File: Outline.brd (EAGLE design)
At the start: 53.8 x 53.8 mm, 51 parts, among them CN1 0675031020, IC1 ATXMEGA32A4U-AU, IC2 ST1480ACDR, J1 RJHSE5080, J2 J2, U1 NCP1117DTAG @ 3.3v, U2 NCP1117DTAG @ 12v

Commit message: 4.1d
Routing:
- net RS485_P: track 68.4 -> 70.6 mm
- net GND: track 16.3 -> 17.0 mm
- net TX: track 10.5 -> 9.92 mm

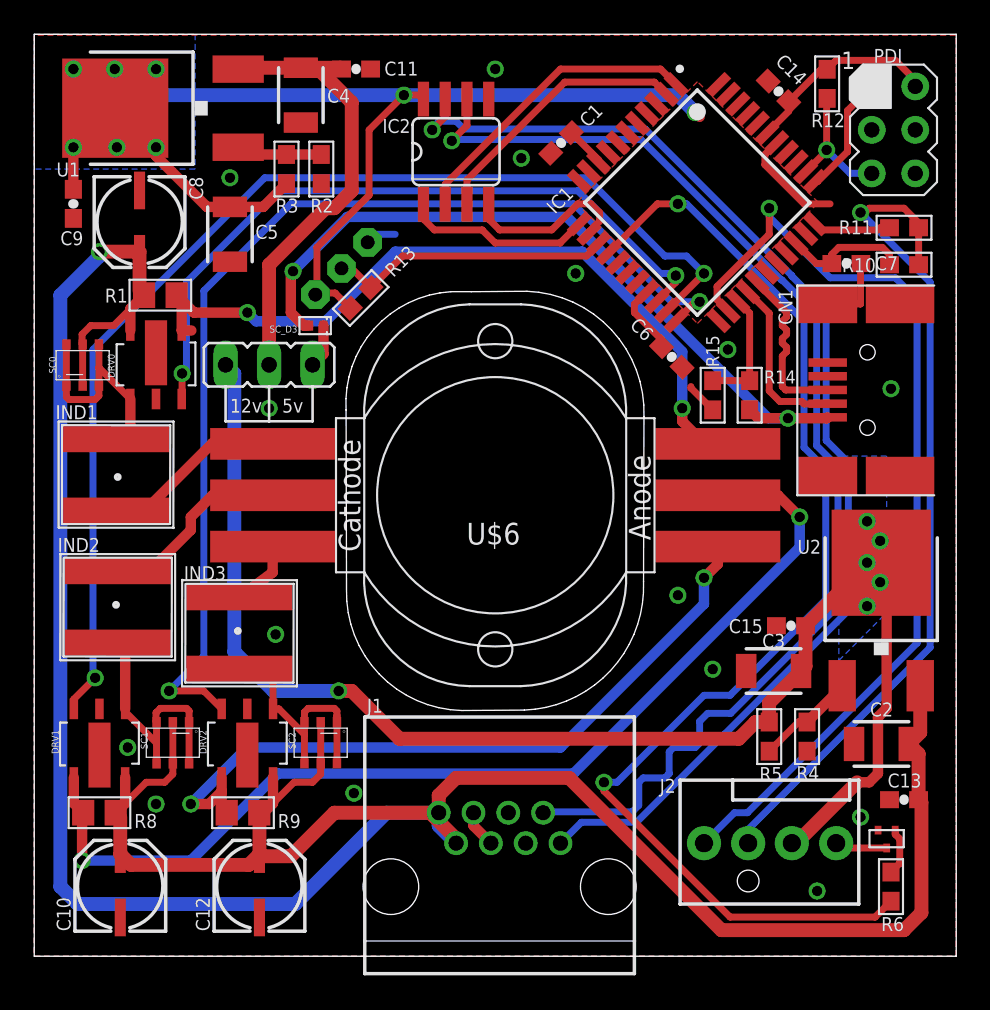
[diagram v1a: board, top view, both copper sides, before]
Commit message: 4.2
Rounded Corners with some final touch up.
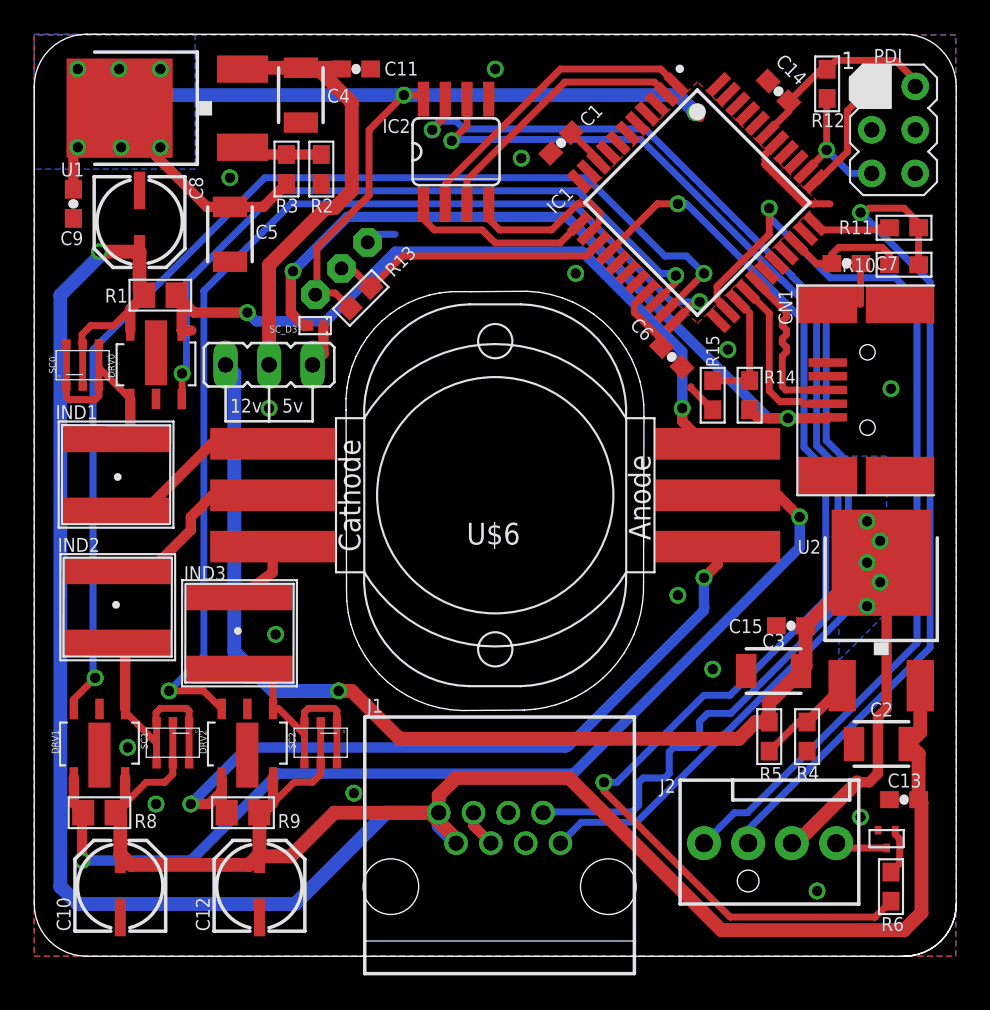
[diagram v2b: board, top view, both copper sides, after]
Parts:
- moved U1 0.25 mm to (7.37, 49.5)
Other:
- outline, holes or cut-outs redrawn
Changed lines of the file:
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@@
 <board>
 <plain>
-<wire x1="0" y1="0" x2="53.848" y2="0" width="0" layer="20"/>
-<wire x1="53.848" y1="0" x2="53.848" y2="53.848" width="0" layer="20"/>
-<wire x1="53.848" y1="53.848" x2="0" y2="53.848" width="0" layer="20"/>
-<wire x1="0" y1="53.848" x2="0" y2="0" width="0" layer="20"/>
+<wire x1="3.048" y1="0" x2="50.8" y2="0" width="0" layer="20"/>
+<wire x1="53.848" y1="3.048" x2="53.848" y2="50.8" width="0" layer="20"/>
+<wire x1="50.8" y1="53.848" x2="3.048" y2="53.848" width="0" layer="20"/>
 <polygon width="0.0508" layer="20" spacing="48.26" pour="hatch">
 <vertex x="25.527" y="38.8112"/>
@@
 <vertex x="50.038" y="49.53"/>
 </polygon>
+<wire x1="0" y1="50.8" x2="0" y2="3.048" width="0" layer="20"/>
 <wire x1="11.176" y1="33.274" x2="11.176" y2="31.242" width="0.1524" layer="25"/>
 <wire x1="13.716" y1="33.274" x2="13.716" y2="31.242" width="0.1524" layer="25"/>
@@
 <text x="11.43" y="31.75" size="0.8128" layer="25">12v</text>
 <text x="14.478" y="31.75" size="0.8128" layer="25">5v</text>
-<text x="3.302" y="46.736" size="1.27" layer="26" font="vector" rot="MR270">http://TechIsCool.com</text>
-<text x="5.334" y="52.832" size="1.27" layer="26" font="vector" rot="MR270">High Brightness RGB LED Driver</text>
-<text x="7.366" y="52.832" size="1.27" layer="26" font="vector" rot="MR270">Copyright 2012 TechIsCool v1.0</text>
+<text x="4.064" y="39.624" size="1.27" layer="26" font="vector" rot="MR270">http://TechIsCool.com</text>
+<text x="5.842" y="46.482" size="1.27" layer="26" font="vector" rot="MR270">High Brightness RGB LED Driver</text>
+<text x="7.62" y="49.022" size="1.27" layer="26" font="vector" rot="MR270">Copyright 2012 TechIsCool v1.0</text>
+<wire x1="0" y1="50.8" x2="3.048" y2="53.848" width="0" layer="20" curve="-90"/>
+<wire x1="53.848" y1="50.8" x2="50.8" y2="53.848" width="0" layer="20" curve="90"/>
+<wire x1="50.8" y1="0" x2="53.848" y2="3.048" width="0" layer="20" curve="90"/>
+<wire x1="50.8" y1="0" x2="53.848" y2="3.048" width="0" layer="20" curve="90"/>
+<wire x1="0" y1="3.048" x2="3.048" y2="0" width="0" layer="20" curve="90"/>
 </plain>
 <attributes>
@@
 <attribute name="NAME" x="12.916" y="41.902" size="0.8128" layer="25"/>
 </element>
-<element name="U1" library="SparkFun" package="V-REG_DPACK" value="NCP1117DTAG @ 3.3v" x="7.112" y="49.53" smashed="yes" rot="R90">
-<attribute name="NAME" x="2.667" y="46.355" size="0.8128" layer="25" rot="R180"/>
+<element name="U1" library="SparkFun" package="V-REG_DPACK" value="NCP1117DTAG @ 3.3v" x="7.366" y="49.53" smashed="yes" rot="R90">
+<attribute name="NAME" x="2.921" y="46.355" size="0.8128" layer="25" rot="R180"/>
 </element>
 <element name="U2" library="SparkFun" package="V-REG_DPACK" value="NCP1117DTAG @ 12v" x="49.4664" y="20.6" smashed="yes">
@@
 <via x="21.59" y="50.292" extent="1-16" drill="0.6"/>
 <wire x1="2.286" y1="44.792" x2="2.286" y2="47.084" width="0.6096" layer="1"/>
-<wire x1="4.732" y1="49.53" x2="4.732" y2="49.116" width="0.6096" layer="1"/>
-<via x="2.286" y="47.244" extent="1-16" drill="0.6"/>
-<via x="4.826" y="47.244" extent="1-16" drill="0.6"/>
-<via x="7.112" y="47.244" extent="1-16" drill="0.6"/>
-<via x="7.112" y="51.816" extent="1-16" drill="0.6"/>
-<via x="4.699" y="51.816" extent="1-16" drill="0.6"/>
-<via x="2.286" y="51.816" extent="1-16" drill="0.6"/>
-<wire x1="2.286" y1="47.084" x2="2.286" y2="47.244" width="0.8128" layer="1"/>
+<wire x1="4.986" y1="49.53" x2="4.732" y2="49.116" width="0.6096" layer="1"/>
+<via x="2.54" y="47.244" extent="1-16" drill="0.6"/>
+<via x="5.08" y="47.244" extent="1-16" drill="0.6"/>
+<via x="7.366" y="47.244" extent="1-16" drill="0.6"/>
+<via x="7.366" y="51.816" extent="1-16" drill="0.6"/>
+<via x="4.953" y="51.816" extent="1-16" drill="0.6"/>
+<via x="2.54" y="51.816" extent="1-16" drill="0.6"/>
+<wire x1="2.286" y1="47.084" x2="2.54" y2="47.244" width="0.8128" layer="1"/>
 <wire x1="46.5821" y1="40.4558125" x2="46.5821" y2="40.9941" width="0.4064" layer="1"/>
 <wire x1="46.5821" y1="40.9941" x2="46.99" y2="41.402" width="0.4064" layer="1"/>
@@
 <wire x1="22.5044" y1="50.292" x2="22.733" y2="50.0634" width="0.4064" layer="1"/>
 <wire x1="10.084" y1="43.764" x2="7.112" y2="46.736" width="0.6096" layer="1"/>
-<wire x1="7.112" y1="46.736" x2="7.112" y2="47.244" width="0.6096" layer="1"/>
+<wire x1="7.112" y1="46.736" x2="7.366" y2="47.244" width="0.6096" layer="1"/>
 <wire x1="16.51" y1="38.734996875" x2="17.572121875" y2="38.734996875" width="0.4064" layer="1"/>
 <wire x1="17.572121875" y1="38.734996875" x2="18.4643625" y2="37.84275625" width="0.4064" layer="1"/>
@@
 <wire x1="19.558" y1="44.45" x2="19.558" y2="48.26" width="0.4064" layer="1"/>
 <wire x1="19.558" y1="48.26" x2="21.59" y2="50.292" width="0.4064" layer="1"/>
-<wire x1="4.826" y1="47.244" x2="4.826" y2="49.436" width="0.4064" layer="1"/>
-<wire x1="4.826" y1="49.436" x2="4.732" y2="49.53" width="0.4064" layer="1"/>
+<wire x1="5.08" y1="47.244" x2="4.826" y2="49.436" width="0.4064" layer="1"/>
+<wire x1="4.826" y1="49.436" x2="4.986" y2="49.53" width="0.4064" layer="1"/>
 <wire x1="37.592" y1="50.292" x2="21.59" y2="50.292" width="0.8128" layer="16"/>
 <wire x1="21.59" y1="50.292" x2="7.112" y2="50.292" width="0.8128" layer="16"/>
-<wire x1="7.112" y1="50.292" x2="7.112" y2="51.816" width="0.8128" layer="16"/>
+<wire x1="7.112" y1="50.292" x2="7.366" y2="51.816" width="0.8128" layer="16"/>
 </signal>
 <signal name="N$1">
@@
 <wire x1="16.764" y1="46.824" x2="14.732" y2="46.824" width="0.6096" layer="1"/>
 <wire x1="14.732" y1="46.824" x2="12.338" y2="46.824" width="0.6096" layer="1"/>
-<wire x1="12.338" y1="46.824" x2="11.912" y2="47.25" width="0.6096" layer="1"/>
+<wire x1="12.338" y1="46.824" x2="12.166" y2="47.25" width="0.6096" layer="1"/>
 </signal>
 <signal name="GND">
@@
 <contactref element="C4" pad="1"/>
 <contactref element="JP1" pad="2"/>
-<wire x1="11.912" y1="51.81" x2="11.9568" y2="51.5112" width="0.6096" layer="1"/>
+<wire x1="12.166" y1="51.81" x2="11.9568" y2="51.5112" width="0.6096" layer="1"/>
 <wire x1="11.9568" y1="51.5112" x2="12.3444" y2="51.5112" width="0.6096" layer="1"/>
 <wire x1="15.5702" y1="51.892" x2="12.248" y2="51.892" width="0.8128" layer="1"/>
-<wire x1="12.248" y1="51.892" x2="11.912" y2="51.81" width="0.6096" layer="1"/>
+<wire x1="12.248" y1="51.892" x2="12.166" y2="51.81" width="0.6096" layer="1"/>
 <contactref element="C11" pad="1"/>
 <wire x1="17.946" y1="51.816" x2="17.87" y2="51.892" width="0.8128" layer="1"/>
@@
 <wire x1="10.946" y1="9.619803125" x2="10.216196875" y2="8.89" width="0.6096" layer="1"/>
 <wire x1="10.216196875" y1="8.89" x2="9.144" y2="8.89" width="0.6096" layer="1"/>
-<wire x1="39.116" y1="20.574" x2="39.116" y2="22.098" width="0.6096" layer="16"/>
-<wire x1="30.734" y1="12.192" x2="12.446" y2="12.192" width="0.6096" layer="16"/>
 <wire x1="12.446" y1="12.192" x2="9.144" y2="8.89" width="0.6096" layer="16"/>
-<wire x1="30.734" y1="12.192" x2="39.116" y2="20.574" width="0.6096" layer="16"/>
+<wire x1="39.116" y1="22.098" x2="39.116" y2="20.425209375" width="0.6096" layer="16"/>
+<wire x1="39.116" y1="20.425209375" x2="39.116" y2="20.32" width="0.6096" layer="16" curve="-44.999502"/>
+<wire x1="39.116" y1="20.32" x2="39.116" y2="20.193" width="0.6096" layer="16"/>
+<wire x1="39.116" y1="20.193" x2="31.18939375" y2="12.26639375" width="0.6096" layer="16"/>
+<wire x1="31.18939375" y1="12.26639375" x2="31.009790625" y2="12.192" width="0.6096" layer="16" curve="-44.999295"/>
+<wire x1="31.009790625" y1="12.192" x2="12.446" y2="12.192" width="0.6096" layer="16"/>
 </signal>
 <signal name="RED_C">

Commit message: 4.2.1
Updated Layout
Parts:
- removed U$6: 10W_RGB_LED, TechIsCool:10W_RGB_LED
- added U$3: 10W_RGB_LED, TechIsCool:10W_LED
- moved R3 1.52 mm to (14.7, 44.5), turned to 180 degrees
- moved R2 1.08 mm to (16.0, 46.7), turned to 180 degrees
- moved C6 0.78 mm to (37.4, 34.2)
- moved R15 0.56 mm to (40.2, 32.8)
- moved R14 0.51 mm to (42.3, 32.8)
- moved C5 0.25 mm to (11.2, 42.2)
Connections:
- net BLUE_A: now also U$3.B$A; no longer U$6.B$2
- net BLUE_C: now also U$3.B$C; no longer U$6.B$1
- net GREEN_A: now also U$3.G$A; no longer U$6.G$2
- net GREEN_C: now also U$3.G$C; no longer U$6.G$1
- net RED_A: now also U$3.R$A; no longer U$6.R$2
- net RED_C: now also U$3.R$C; no longer U$6.R$1
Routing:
- net +5V: track 43.9 -> 41.2 mm
- net GND: track 17.0 -> 15.2 mm
- net FAN_SWITCH: track 70.3 -> 69.4 mm
- net USB+: track 10.1 -> 9.28 mm
- net N$1: track 4.89 -> 5.66 mm

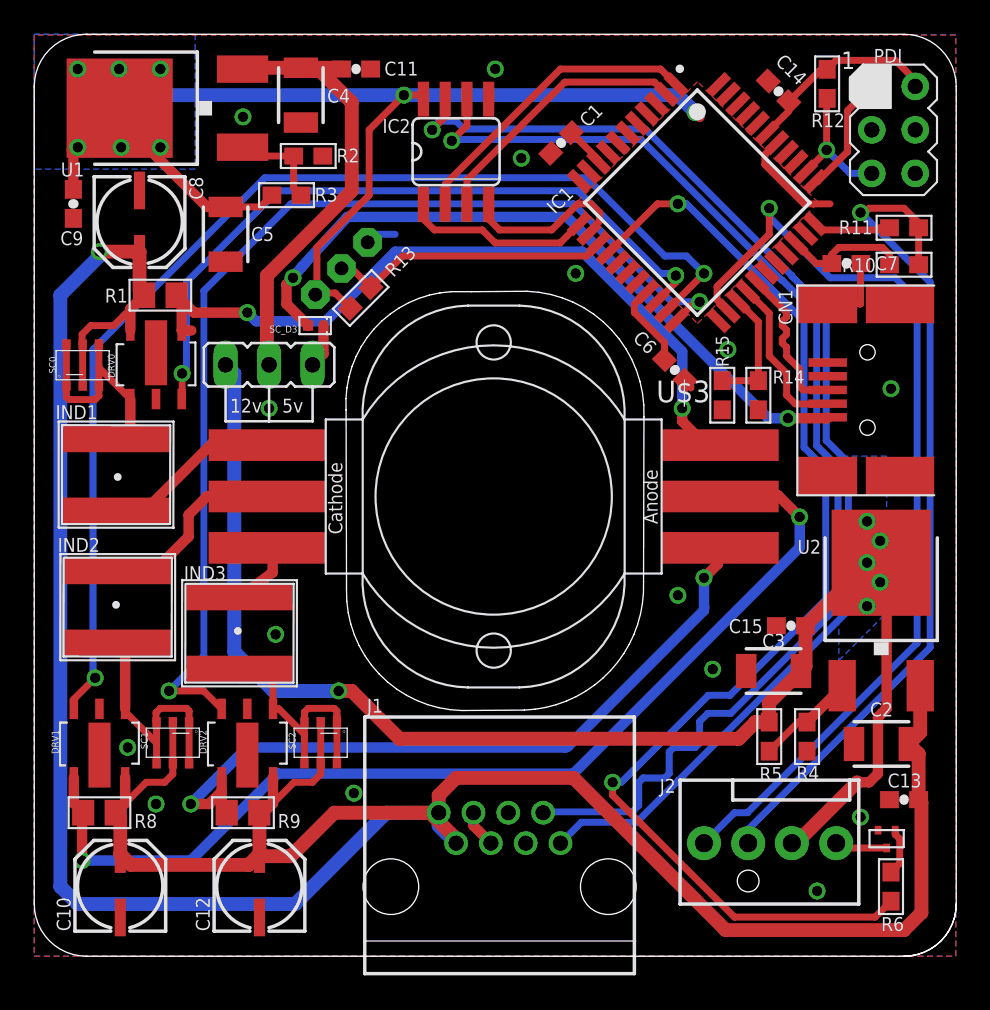
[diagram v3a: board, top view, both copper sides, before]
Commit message: 4.2.2
Connected a few things and add a via. Also gnded the extra wires in the
RJ45 cable
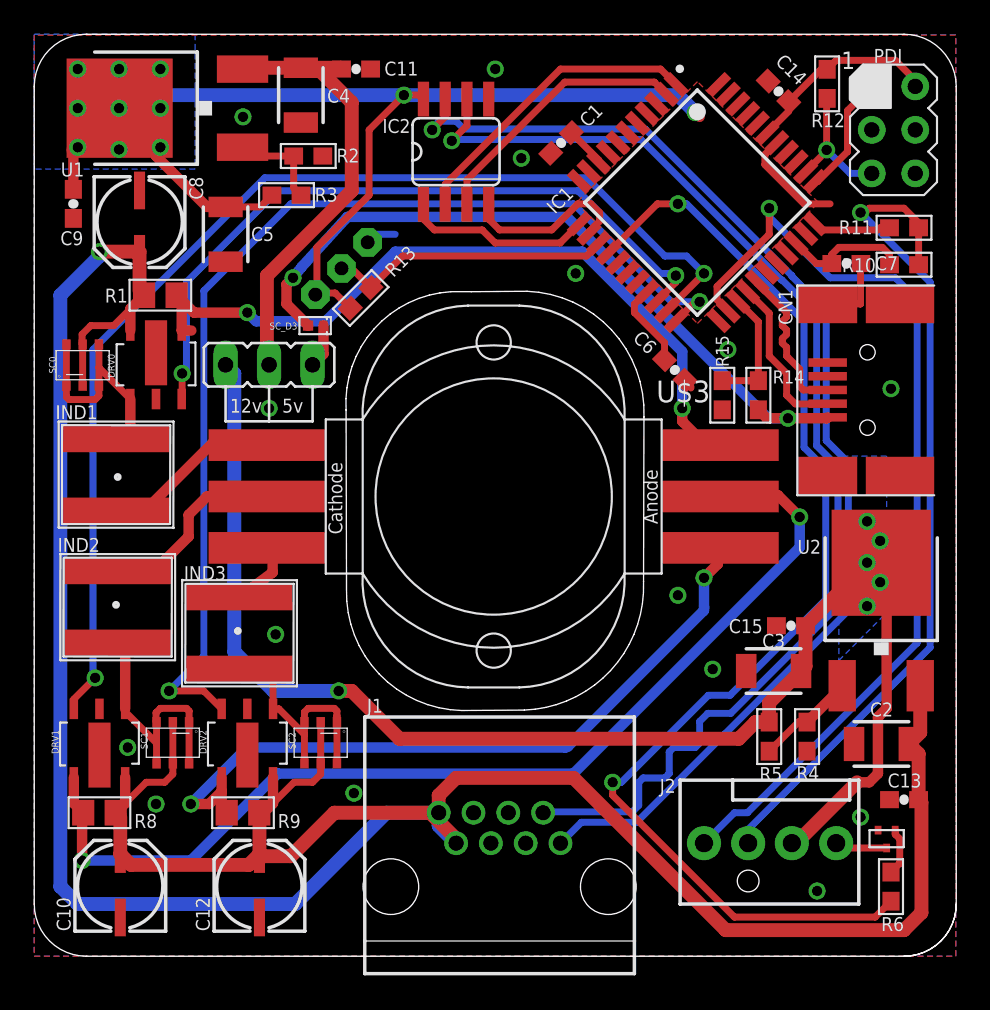
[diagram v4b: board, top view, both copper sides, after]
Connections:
- net GND: now also J1.P$3, J1.P$4
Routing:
- net GND: track 15.2 -> 13.0 mm
- net +5V: track 41.2 -> 43.1 mm
- net +3V3: track 91.9 -> 92.0 mm, vias 8 -> 11
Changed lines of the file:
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@@
 </element>
 <element name="SC_D3" library="TechIsCool" package="NSR05F20" value="1PS74SB23" x="16.891" y="36.83" smashed="yes" rot="R180">
-<attribute name="NAME" x="15.367" y="36.83" size="0.4064" layer="25" rot="R180"/>
+<attribute name="NAME" x="15.367" y="37.0078" size="0.4064" layer="25" rot="R180"/>
 </element>
 <element name="U$3" library="TechIsCool" package="10W_LED" value="10W_RGB_LED" x="27.0256" y="26.5684" smashed="yes">
@@
 <wire x1="4.986" y1="49.53" x2="4.732" y2="49.116" width="0.6096" layer="1"/>
 <via x="2.54" y="47.244" extent="1-16" drill="0.6"/>
-<via x="5.08" y="47.244" extent="1-16" drill="0.6"/>
+<via x="4.953" y="47.117" extent="1-16" drill="0.6"/>
 <via x="7.366" y="47.244" extent="1-16" drill="0.6"/>
 <via x="7.366" y="51.816" extent="1-16" drill="0.6"/>
@@
 <wire x1="19.558" y1="44.45" x2="19.558" y2="48.26" width="0.4064" layer="1"/>
 <wire x1="19.558" y1="48.26" x2="21.59" y2="50.292" width="0.4064" layer="1"/>
-<wire x1="5.08" y1="47.244" x2="4.826" y2="49.436" width="0.4064" layer="1"/>
+<wire x1="4.953" y1="47.117" x2="4.826" y2="49.436" width="0.4064" layer="1"/>
 <wire x1="4.826" y1="49.436" x2="4.986" y2="49.53" width="0.4064" layer="1"/>
 <wire x1="37.592" y1="50.292" x2="21.59" y2="50.292" width="0.8128" layer="16"/>
@@
 <wire x1="13.196" y1="43.764" x2="13.882" y2="44.45" width="0.4064" layer="1"/>
 <wire x1="36.811353125" y1="35.832646875" x2="36.811353125" y2="34.842046875" width="0.4064" layer="1"/>
+<via x="2.54" y="49.53" extent="1-16" drill="0.6"/>
+<via x="4.953" y="49.53" extent="1-16" drill="0.6"/>
+<via x="7.366" y="49.53" extent="1-16" drill="0.6"/>
 </signal>
 <signal name="N$1">
@@
 <contactref element="U$1" pad="P$S"/>
 <via x="48.26" y="8.128" extent="1-16" drill="0.6"/>
-<wire x1="25.654" y1="8.382" x2="25.654" y2="7.62" width="0.6096" layer="1"/>
-<wire x1="25.654" y1="7.62" x2="26.67" y2="6.604" width="0.6096" layer="1"/>
 <via x="45.72" y="3.81" extent="1-16" drill="0.6"/>
 <wire x1="48.2821" y1="40.4558125" x2="48.26" y2="40.4337125" width="0.4064" layer="1"/>
@@
 <wire x1="19.47084375" y1="41.695840625" x2="19.939003125" y2="42.164" width="0.4064" layer="16"/>
 <wire x1="19.939003125" y1="42.164" x2="21.082" y2="42.164" width="0.4064" layer="16"/>
+<contactref element="J1" pad="P$4"/>
+<contactref element="J1" pad="P$3"/>
 </signal>
 <signal name="+12V">
@@
 <wire x1="14.732" y1="38.1" x2="14.732" y2="39.243" width="0.6096" layer="1"/>
 <wire x1="14.732" y1="39.243" x2="15.113" y2="39.624" width="0.6096" layer="1"/>
-<wire x1="42.8752" y1="31.4198" x2="42.291" y2="31.916" width="0" layer="19" extent="1-16"/>
+<wire x1="42.291" y1="31.916" x2="42.7872" y2="31.4198" width="0.6096" layer="1"/>
+<wire x1="42.7872" y1="31.4198" x2="44.0182" y2="31.4198" width="0.6096" layer="1"/>
 </signal>
 <signal name="N$22">
